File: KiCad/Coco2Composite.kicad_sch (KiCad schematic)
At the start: 19 parts, among them J1 MA03-1, J2 MA05-1, J3 AUDIO_JACK_3.5MM_PTH, Q1 PN2907, Q2 2N2222, U1 MC1372

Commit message: Updated KiCad based on board schematic
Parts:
- R1, R4, R5, R6, R7: footprint Resistor_THT:R_Axial_DIN0204_L3.6mm_D1.6mm_P2.54mm_Vertical -> Resistor_THT:R_Axial_DIN0204_L3.6mm_D1.6mm_P5.08mm_Horizontal
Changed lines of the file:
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@@
 			)
 		)
-		(property "Footprint" "Resistor_THT:R_Axial_DIN0204_L3.6mm_D1.6mm_P2.54mm_Vertical"
+		(property "Footprint" "Resistor_THT:R_Axial_DIN0204_L3.6mm_D1.6mm_P5.08mm_Horizontal"
 			(at 220.98 114.3 0)
 			(effects
@@
 			)
 		)
-		(property "Footprint" "Resistor_THT:R_Axial_DIN0204_L3.6mm_D1.6mm_P2.54mm_Vertical"
+		(property "Footprint" "Resistor_THT:R_Axial_DIN0204_L3.6mm_D1.6mm_P5.08mm_Horizontal"
 			(at 185.42 114.3 0)
 			(effects
@@
 			)
 		)
-		(property "Footprint" "Resistor_THT:R_Axial_DIN0204_L3.6mm_D1.6mm_P2.54mm_Vertical"
+		(property "Footprint" "Resistor_THT:R_Axial_DIN0204_L3.6mm_D1.6mm_P5.08mm_Horizontal"
 			(at 134.62 58.42 0)
 			(effects
@@
 			)
 		)
-		(property "Footprint" "Resistor_THT:R_Axial_DIN0204_L3.6mm_D1.6mm_P2.54mm_Vertical"
+		(property "Footprint" "Resistor_THT:R_Axial_DIN0204_L3.6mm_D1.6mm_P5.08mm_Horizontal"
 			(at 200.66 121.92 0)
 			(effects
@@
 			)
 		)
-		(property "Footprint" "Resistor_THT:R_Axial_DIN0204_L3.6mm_D1.6mm_P2.54mm_Vertical"
+		(property "Footprint" "Resistor_THT:R_Axial_DIN0204_L3.6mm_D1.6mm_P5.08mm_Horizontal"
 			(at 238.76 121.92 0)
 			(effects

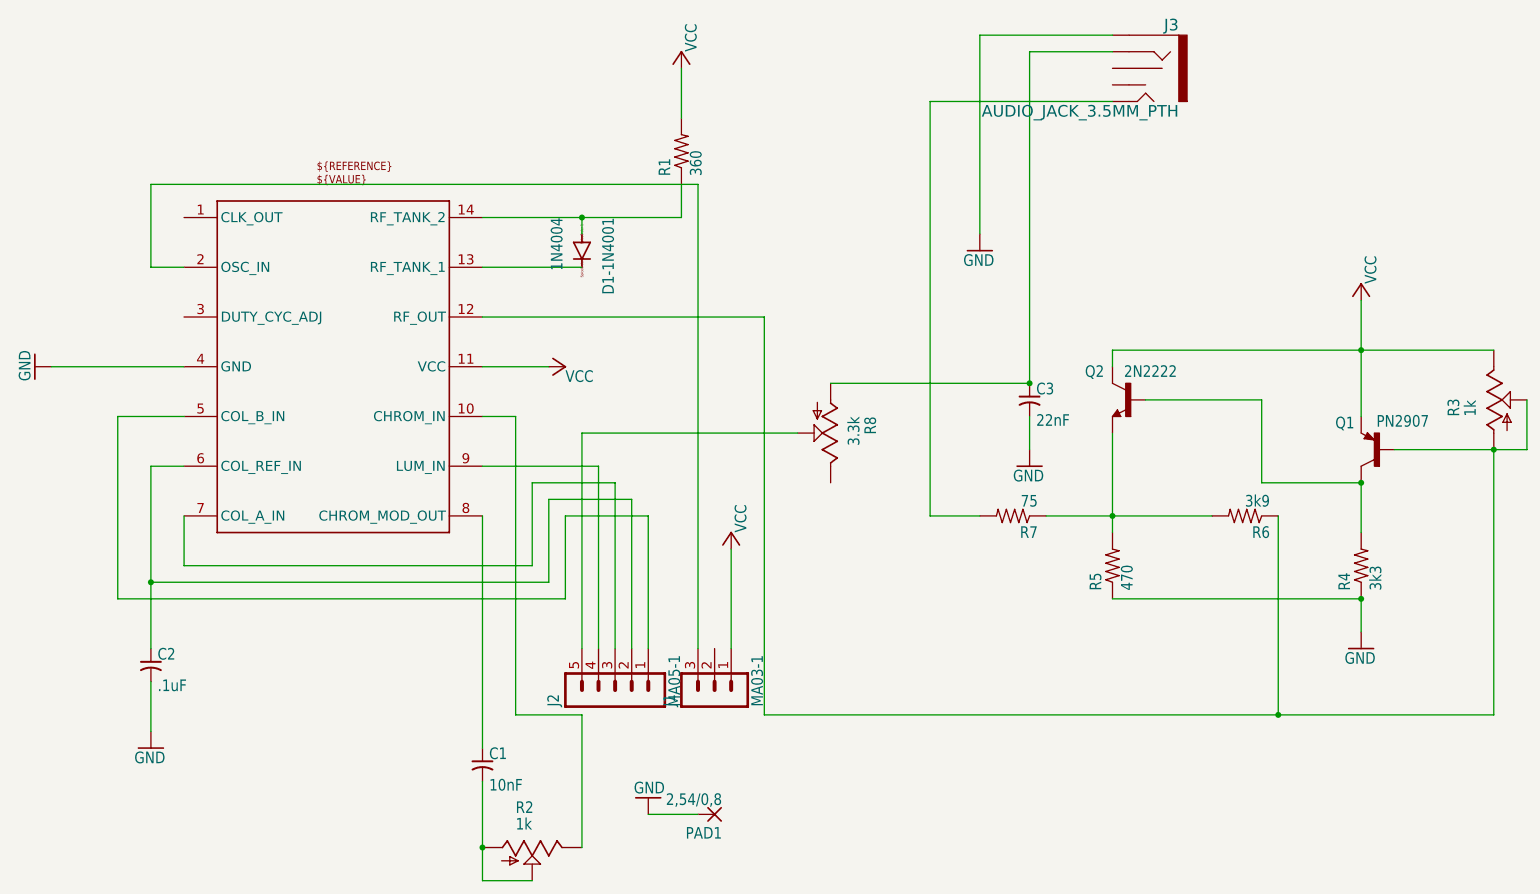
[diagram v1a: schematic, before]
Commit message: moved ground pad to hopefully have it work as a support strut anchor point
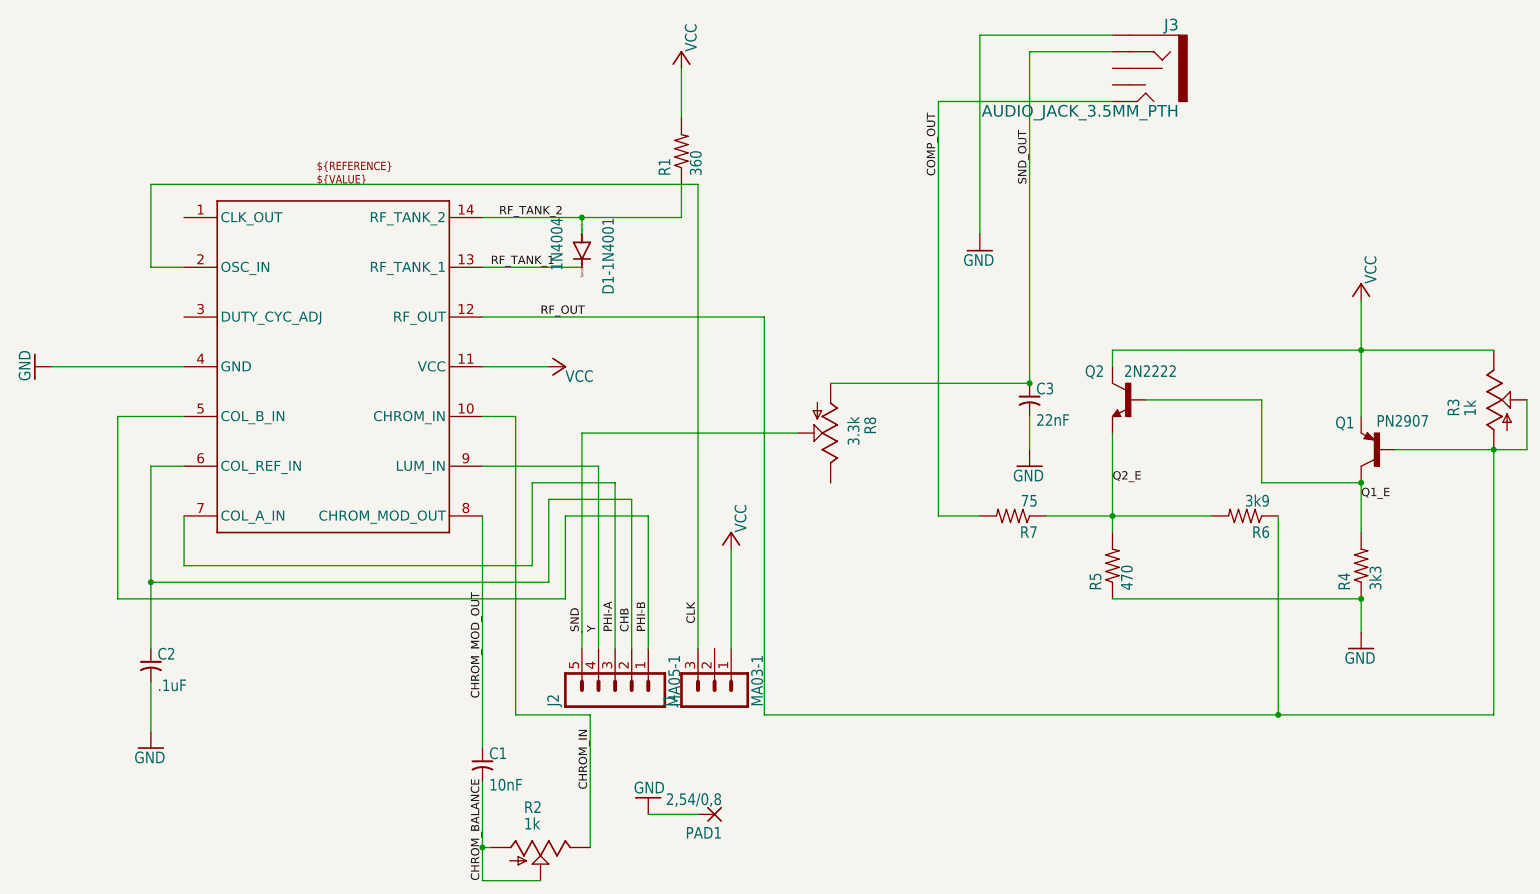
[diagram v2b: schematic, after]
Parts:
- PAD1: footprint TestPoint:TestPoint_THTPad_2.0x2.0mm_Drill1.0mm -> MountingHole:MountingHole_2.2mm_M2_DIN965_Pad
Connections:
- net RF_OUT: now reaches Q1.B, R3.A, R3.S, R6.1, U1.12 (RF_OUT)
- net Q2_E: now reaches Q2.1 (E), R5.2, R6.2, R7.1
- net PHI-B: now reaches J2.1, U1.5 (COL_B_IN)
- net CHB: now reaches C2.1, J2.2, U1.6 (COL_REF_IN)
- net PHI-A: now reaches J2.3, U1.7 (COL_A_IN)
- net Y: now reaches J2.4, U1.9 (LUM_IN)
- net SND: now reaches J2.5, R8.S
- net SND_OUT: now reaches C3.1, J3.RING, R8.A
- net COMP_OUT: now reaches J3.TIP, R7.2
- net Q1_E: now reaches Q1.C, Q2.2 (B), R4.2
- net RF_TANK_2: now reaches D1-1N4001.A, R1.1, U1.14 (RF_TANK_2)
- net RF_TANK_1: now reaches D1-1N4001.C, U1.13 (RF_TANK_1)
- net CHROM_BALANCE: now reaches C1.2, R2.A, R2.S
- net CHROM_IN: now reaches R2.E, U1.10 (CHROM_IN)
- net CLK: now reaches J1.3, U1.2 (OSC_IN)
- net CHROM_MOD_OUT: now reaches C1.1, U1.8 (CHROM_MOD_OUT)
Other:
- moved on the sheet: R2

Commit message: Minor tweaks
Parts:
- PAD1: footprint MountingHole:MountingHole_2.2mm_M2_DIN965_Pad -> MountingHole:MountingHole_3.7mm_Pad
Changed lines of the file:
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@@
 			)
 		)
-		(property "Footprint" "MountingHole:MountingHole_2.2mm_M2_DIN965_Pad"
+		(property "Footprint" "MountingHole:MountingHole_3.7mm_Pad"
 			(at 139.7 160.02 0)
 			(effects
